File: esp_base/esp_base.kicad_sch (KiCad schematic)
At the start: 16 parts, among them J1 Conn_01x02_Pin, J2 Conn_01x02_Pin, J3 Conn_01x02_Pin, U1 ESP32-C3-WROOM-02, U2 AP2112K-3.3

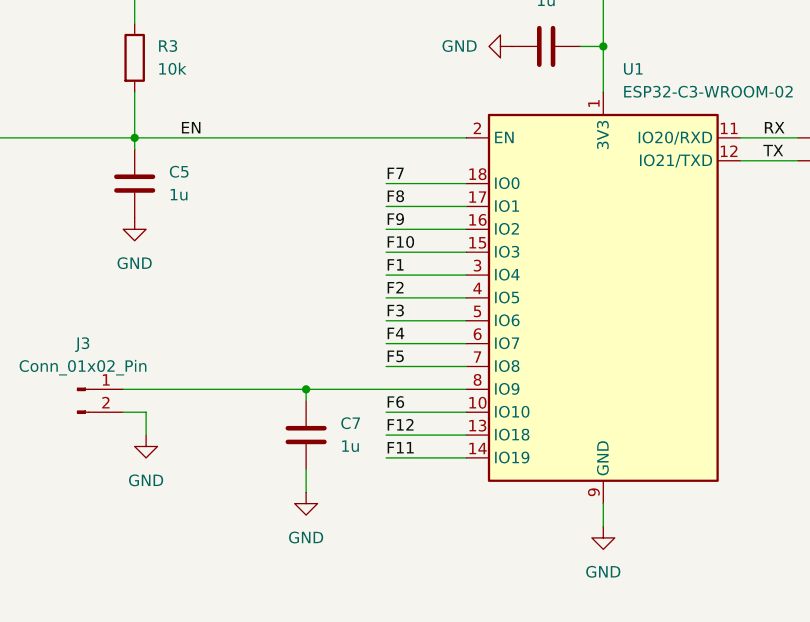
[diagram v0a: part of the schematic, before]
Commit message: komponent moved to new position smaller eddition
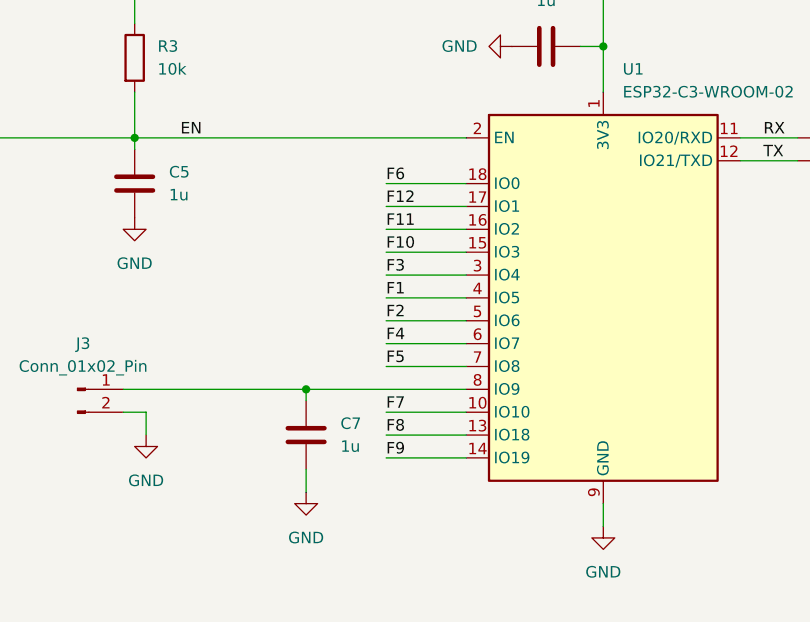
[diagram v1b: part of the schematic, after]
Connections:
- net F1: now also U1.4 (IO5); no longer U1.3 (IO4)
- net F11: now also U1.16 (IO2); no longer U1.14 (IO19)
- net F12: now also U1.17 (IO1); no longer U1.13 (IO18)
- net F2: now also U1.5 (IO6); no longer U1.4 (IO5)
- net F3: now also U1.3 (IO4); no longer U1.5 (IO6)
- net F6: now also U1.18 (IO0); no longer U1.10 (IO10)
- net F7: now also U1.10 (IO10); no longer U1.18 (IO0)
- net F8: now also U1.13 (IO18); no longer U1.17 (IO1)
- net F9: now also U1.14 (IO19); no longer U1.16 (IO2)
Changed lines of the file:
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@@
 	)
 	(label "F1"
-		(at 138.43 76.2 0)
+		(at 138.43 78.74 0)
 		(effects
 			(font
@@
 	)
 	(label "F12"
-		(at 138.43 93.98 0)
+		(at 138.43 68.58 0)
 		(effects
 			(font
@@
 	)
 	(label "F8"
-		(at 138.43 68.58 0)
+		(at 138.43 93.98 0)
 		(effects
 			(font
@@
 	)
 	(label "F3"
-		(at 138.43 81.28 0)
+		(at 138.43 76.2 0)
 		(effects
 			(font
@@
 	)
 	(label "F7"
-		(at 138.43 66.04 0)
+		(at 138.43 91.44 0)
 		(effects
 			(font
@@
 	)
 	(label "F11"
-		(at 138.43 96.52 0)
+		(at 138.43 71.12 0)
 		(effects
 			(font
@@
 	)
 	(label "F6"
-		(at 138.43 91.44 0)
+		(at 138.43 66.04 0)
 		(effects
 			(font
@@
 	)
 	(label "F9"
-		(at 138.43 71.12 0)
+		(at 138.43 96.52 0)
 		(effects
 			(font
@@
 	)
 	(label "F2"
-		(at 138.43 78.74 0)
+		(at 138.43 81.28 0)
 		(effects
 			(font

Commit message: NEW PADS
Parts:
- removed 5V1, GND1: TestPoint_Alt, TestPoint:TestPoint_THTPad_D2.0mm_Drill1.0mm, symbol Connector:TestPoint_Alt
- added 5V, GND: TestPoint_Alt, TestPoint:TestPoint_Pad_2.0x2.0mm, symbol Connector:TestPoint_Alt
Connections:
- net +5V: now also 5V.1
- net GND: now also GND.1
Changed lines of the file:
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@@
+	)
+	(symbol
+		(lib_id "power:GND")
+		(at 129.54 100.33 0)
+		(unit 1)
+		(exclude_from_sim no)
+		(in_bom yes)
+		(on_board yes)
+		(dnp no)
+		(fields_autoplaced yes)
+		(property "Reference" "#PWR012"
+			(at 129.54 106.68 0)
+			(effects
+				(font
+					(size 1.27 1.27)
+				)
+				(hide yes)
+			)
+		)
+		(property "Value" "GND"
+			(at 129.54 105.41 0)
+			(effects
+				(font
+					(size 1.27 1.27)
+				)
+			)
+		)
+		(property "Footprint" ""
+			(at 129.54 100.33 0)
+			(effects
+				(font
+					(size 1.27 1.27)
+				)
+				(hide yes)
+			)
+		)
+		(property "Datasheet" ""
+			(at 129.54 100.33 0)
+			(effects
+				(font
+					(size 1.27 1.27)
+				)
+				(hide yes)
+			)
+		)
+		(property "Description" "Power symbol creates a global label with name \"GND\" , ground"
+			(at 129.54 100.33 0)
+			(effects
+				(font
+					(size 1.27 1.27)
+				)
+				(hide yes)
+			)
+		)
+		(pin "1"
+		)
+		(instances
+			(project "esp_base"
+				(path "/b9883b8e-181f-47a1-bc04-7eade380b6a1"
+					(reference "#PWR012")
+					(unit 1)
+				)
+			)
+		)
+	)
+	(symbol
+		(lib_id "Device:C")
+		(at 77.47 44.45 0)
+		(unit 1)
+		(exclude_from_sim no)
+		(in_bom yes)
+		(on_board yes)
+		(dnp no)
+		(fields_autoplaced yes)
+		(property "Reference" "C2"
+			(at 81.28 43.1799 0)
+			(effects
+				(font
+					(size 1.27 1.27)
+				)
+				(justify left)
+			)
+		)
+		(property "Value" "1u"
+			(at 81.28 45.7199 0)
+			(effects
+				(font
+					(size 1.27 1.27)
+				)
+				(justify left)
+			)
+		)
+		(property "Footprint" "Capacitor_SMD:C_0805_2012Metric"
+			(at 78.4352 48.26 0)
+			(effects
+				(font
+					(size 1.27 1.27)
+				)
+				(hide yes)
+			)
+		)
+		(property "Datasheet" "~"
+			(at 77.47 44.45 0)
+			(effects
+				(font
+					(size 1.27 1.27)
+				)
+				(hide yes)
+			)
+		)
+		(property "Description" "Unpolarized capacitor"
+			(at 77.47 44.45 0)
+			(effects
+				(font
+					(size 1.27 1.27)
+				)
+				(hide yes)
+			)
+		)
+		(pin "1"
+		)
+		(pin "2"
+		)
+		(instances
+			(project "esp_base"
+				(path "/b9883b8e-181f-47a1-bc04-7eade380b6a1"
+					(reference "C2")
+					(unit 1)
+				)
+			)
+		)
+	)
+	(symbol
+		(lib_id "power:GND")
+		(at 162.56 104.14 0)
+		(unit 1)
+		(exclude_from_sim no)
+		(in_bom yes)
+		(on_board yes)
+		(dnp no)
+		(fields_autoplaced yes)
+		(property "Reference" "#PWR01"
+			(at 162.56 110.49 0)
+			(effects
+				(font
+					(size 1.27 1.27)
+				)
+				(hide yes)
+			)
+		)
+		(property "Value" "GND"
+			(at 162.56 109.22 0)
+			(effects
+				(font
+					(size 1.27 1.27)
+				)
+			)
+		)
+		(property "Footprint" ""
+			(at 162.56 104.14 0)
+			(effects
+				(font
+					(size 1.27 1.27)
+				)
+				(hide yes)
+			)
+		)
+		(property "Datasheet" ""
+			(at 162.56 104.14 0)
+			(effects
+				(font
+					(size 1.27 1.27)
+				)
+				(hide yes)
+			)
+		)
+		(property "Description" "Power symbol creates a global label with name \"GND\" , ground"
+			(at 162.56 104.14 0)
+			(effects
+				(font
+					(size 1.27 1.27)
+				)
+				(hide yes)
+			)
+		)
+		(pin "1"
+		)
+		(instances
+			(project ""
+				(path "/b9883b8e-181f-47a1-bc04-7eade380b6a1"
+					(reference "#PWR01")
+					(unit 1)
+				)
+			)
+		)
 	)
 	(symbol
@@
 		(dnp no)
 		(fields_autoplaced yes)
-		(property "Reference" "GND1"
-			(at 101.6 117.3479 0)
+		(property "Reference" "GND"
+			(at 101.6 118.6179 0)
 			(effects
 				(font
@@
 				)
 				(justify left)
-			)
-		)
-		(property "Footprint" "TestPoint:TestPoint_THTPad_D2.0mm_Drill1.0mm"
+				(hide yes)
+			)
+		)
+		(property "Footprint" "TestPoint:TestPoint_Pad_2.0x2.0mm"
 			(at 104.14 121.92 0)
 			(effects
@@
 			(project "esp_base"
 				(path "/b9883b8e-181f-47a1-bc04-7eade380b6a1"
-					(reference "GND1")
-					(unit 1)
-				)
-			)
-		)
-	)
-	(symbol
-		(lib_id "power:GND")
-		(at 129.54 100.33 0)
-		(unit 1)
-		(exclude_from_sim no)
-		(in_bom yes)
-		(on_board yes)
-		(dnp no)
-		(fields_autoplaced yes)
-		(property "Reference" "#PWR012"
-			(at 129.54 106.68 0)
-			(effects
-				(font
-					(size 1.27 1.27)
-				)
-				(hide yes)
-			)
-		)
-		(property "Value" "GND"
-			(at 129.54 105.41 0)
-			(effects
-				(font
-					(size 1.27 1.27)
-				)
-			)
-		)
-		(property "Footprint" ""
-			(at 129.54 100.33 0)
-			(effects
-				(font
-					(size 1.27 1.27)
-				)
-				(hide yes)
-			)
-		)
-		(property "Datasheet" ""
-			(at 129.54 100.33 0)
-			(effects
-				(font
-					(size 1.27 1.27)
-				)
-				(hide yes)
-			)
-		)
-		(property "Description" "Power symbol creates a global label with name \"GND\" , ground"
-			(at 129.54 100.33 0)
-			(effects
-				(font
-					(size 1.27 1.27)
-				)
-				(hide yes)
-			)
-		)
-		(pin "1"
-		)
-		(instances
-			(project "esp_base"
-				(path "/b9883b8e-181f-47a1-bc04-7eade380b6a1"
-					(reference "#PWR012")
-					(unit 1)
-				)
-			)
-		)
-	)
-	(symbol
-		(lib_id "Device:C")
-		(at 77.47 44.45 0)
-		(unit 1)
-		(exclude_from_sim no)
-		(in_bom yes)
-		(on_board yes)
-		(dnp no)
-		(fields_autoplaced yes)
-		(property "Reference" "C2"
-			(at 81.28 43.1799 0)
-			(effects
-				(font
-					(size 1.27 1.27)
-				)
-				(justify left)
-			)
-		)
-		(property "Value" "1u"
-			(at 81.28 45.7199 0)
-			(effects
-				(font
-					(size 1.27 1.27)
-				)
-				(justify left)
-			)
-		)
-		(property "Footprint" "Capacitor_SMD:C_0805_2012Metric"
-			(at 78.4352 48.26 0)
-			(effects
-				(font
-					(size 1.27 1.27)
-				)
-				(hide yes)
-			)
-		)
-		(property "Datasheet" "~"
-			(at 77.47 44.45 0)
-			(effects
-				(font
-					(size 1.27 1.27)
-				)
-				(hide yes)
-			)
-		)
-		(property "Description" "Unpolarized capacitor"
-			(at 77.47 44.45 0)
-			(effects
-				(font
-					(size 1.27 1.27)
-				)
-				(hide yes)
-			)
-		)
-		(pin "1"
-		)
-		(pin "2"
-		)
-		(instances
-			(project "esp_base"
-				(path "/b9883b8e-181f-47a1-bc04-7eade380b6a1"
-					(reference "C2")
-					(unit 1)
-				)
-			)
-		)
-	)
-	(symbol
-		(lib_id "power:GND")
-		(at 162.56 104.14 0)
-		(unit 1)
-		(exclude_from_sim no)
-		(in_bom yes)
-		(on_board yes)
-		(dnp no)
-		(fields_autoplaced yes)
-		(property "Reference" "#PWR01"
-			(at 162.56 110.49 0)
-			(effects
-				(font
-					(size 1.27 1.27)
-				)
-				(hide yes)
-			)
-		)
-		(property "Value" "GND"
-			(at 162.56 109.22 0)
-			(effects
-				(font
-					(size 1.27 1.27)
-				)
-			)
-		)
-		(property "Footprint" ""
-			(at 162.56 104.14 0)
-			(effects
-				(font
-					(size 1.27 1.27)
-				)
-				(hide yes)
-			)
-		)
-		(property "Datasheet" ""
-			(at 162.56 104.14 0)
-			(effects
-				(font
-					(size 1.27 1.27)
-				)
-				(hide yes)
-			)
-		)
-		(property "Description" "Power symbol creates a global label with name \"GND\" , ground"
-			(at 162.56 104.14 0)
-			(effects
-				(font
-					(size 1.27 1.27)
-				)
-				(hide yes)
-			)
-		)
-		(pin "1"
-		)
-		(instances
-			(project ""
-				(path "/b9883b8e-181f-47a1-bc04-7eade380b6a1"
-					(reference "#PWR01")
+					(reference "GND")
 					(unit 1)
 				)
@@
 		(dnp no)
 		(fields_autoplaced yes)
-		(property "Reference" "5V1"
-			(at 43.18 32.2579 0)
+		(property "Reference" "5V"
+			(at 43.18 33.5279 0)
 			(effects
 				(font
@@
 				)
 				(justify left)
-			)
-		)
-		(property "Footprint" "TestPoint:TestPoint_THTPad_D2.0mm_Drill1.0mm"
+				(hide yes)
+			)
+		)
+		(property "Footprint" "TestPoint:TestPoint_Pad_2.0x2.0mm"
 			(at 45.72 36.83 0)
 			(effects
@@
 			(project "esp_base"
 				(path "/b9883b8e-181f-47a1-bc04-7eade380b6a1"
-					(reference "5V1")
-					(unit 1)
-				)
+					(reference "5V")
+					(unit 1)
+				)

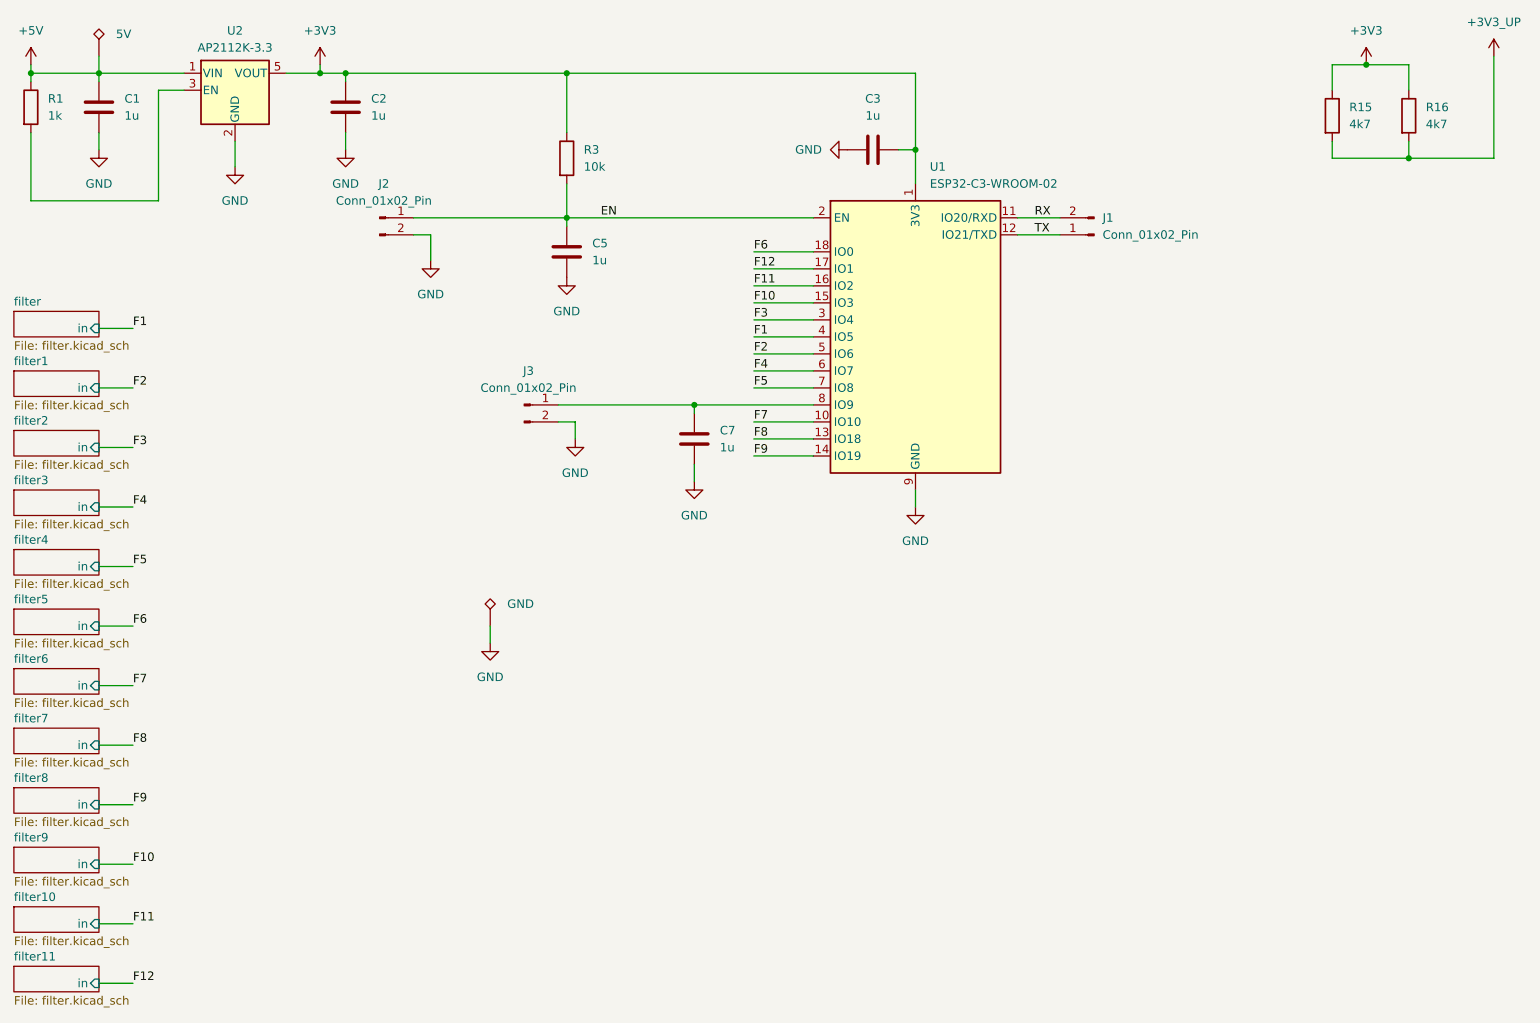
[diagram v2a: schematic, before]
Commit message: last version with cahges on pull up resistor
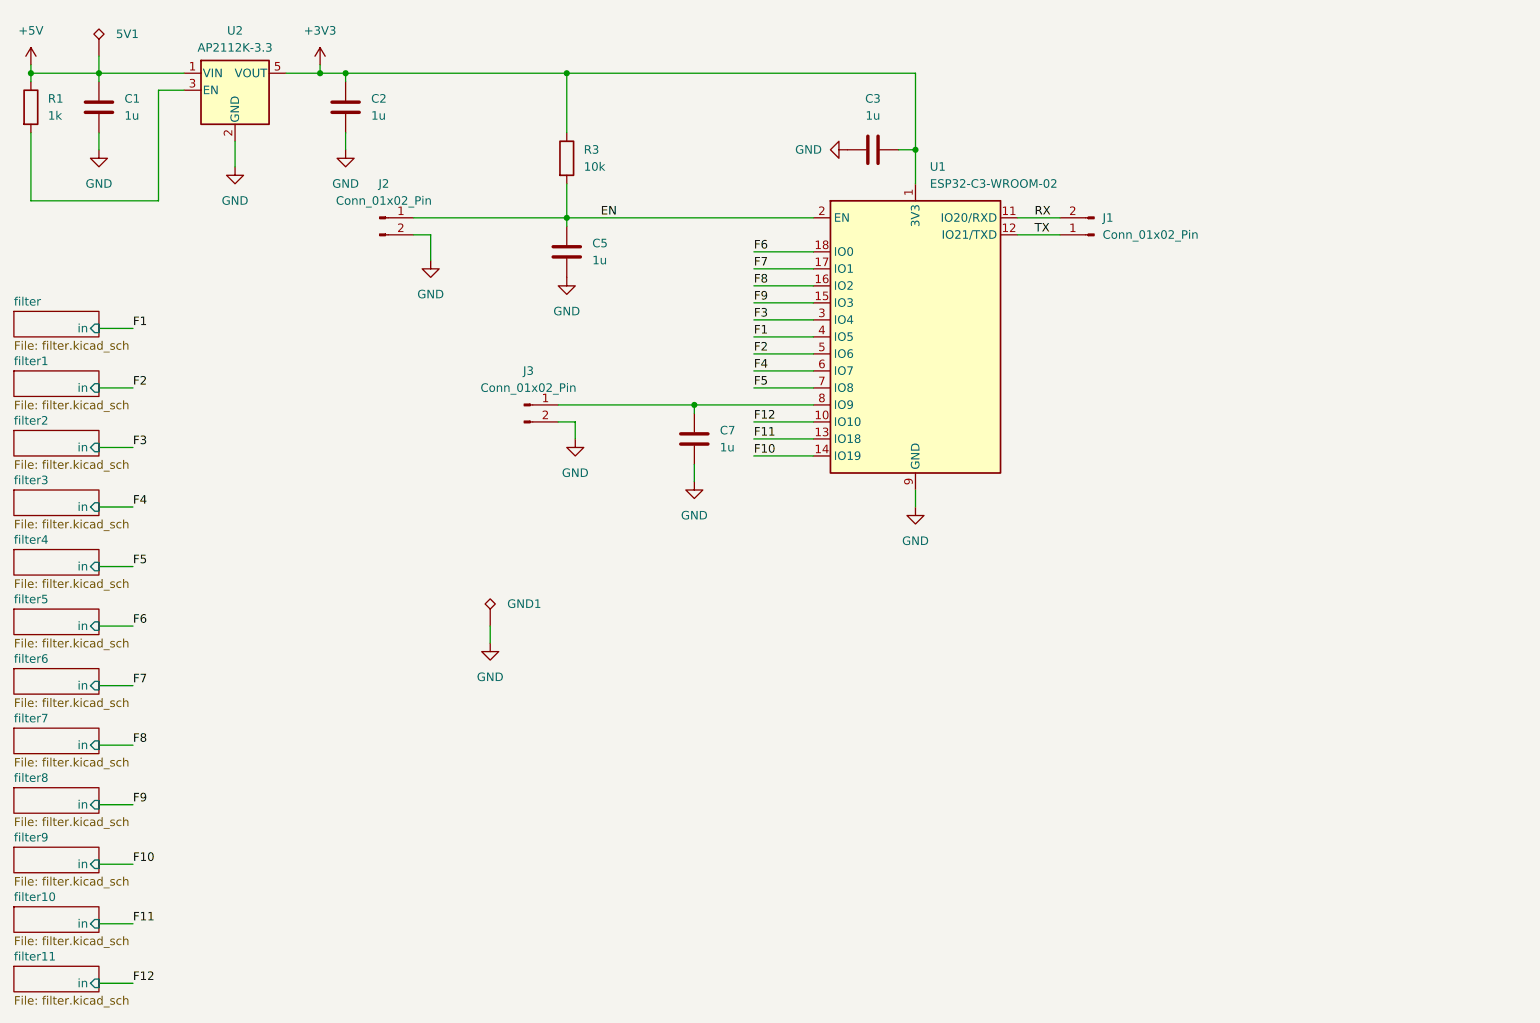
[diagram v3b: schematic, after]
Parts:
- removed R15, R16: 4k7, Resistor_SMD:R_0805_2012Metric, symbol Device:R
- renumbered 5V to 5V1, GND to GND1
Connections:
- net F10: now also U1.14 (IO19); no longer U1.15 (IO3)
- net F11: now also U1.13 (IO18); no longer U1.16 (IO2)
- net F12: now also U1.10 (IO10); no longer U1.17 (IO1)
- net F7: now also U1.17 (IO1); no longer U1.10 (IO10)
- net F8: now also U1.16 (IO2); no longer U1.13 (IO18)
- net F9: now also U1.15 (IO3); no longer U1.14 (IO19)
